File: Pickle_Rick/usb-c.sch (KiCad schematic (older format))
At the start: 3 parts

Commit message: updated optocoupler, usb kinda weird atm ¯\_(ツ)_/¯
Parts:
- removed J?: USB_C_Receptacle_USB2.0, symbol Connector:USB_C_Receptacle_USB2.0
- added R? (x2): 5.1k, symbol Device:R
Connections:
- net labels added: usb_DETONATOR
- net labels removed: usb_ID
- wire segments 24 -> 21
- no-connect marks 4 -> 2
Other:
- note added: "How it was before"
- note added: "Might do a thing..."
- note added: "d+"
- note added: "d-"
- note added: "detonator\n"
- note added: "tought id was for "device identification"?\n"
- note added: "vbus"
- note removed: "One of these is right for sure..."
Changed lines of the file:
@@
 L Connector:USB_B_Micro J?
 U 1 1 6049A0C6
-P 2100 3650
+P 1550 3050
 AR Path="/6049A0C6" Ref="J?"  Part="1"
 AR Path="/602F075A/6049A0C6" Ref="J?"  Part="1"
-F 0 "J?" H 2157 4117 50  0000 C CNN
-F 1 "USB_B_Micro" H 2157 4026 50  0000 C CNN
-F 2 "Connector_USB:USB_Micro-B_Amphenol_10103594-0001LF_Horizontal" H 2250 3600 50  0001 C CNN
-F 3 "~" H 2250 3600 50  0001 C CNN
-	1    2100 3650
+F 0 "J?" H 1607 3517 50  0000 C CNN
+F 1 "USB_B_Micro" H 1607 3426 50  0000 C CNN
+F 2 "Connector_USB:USB_Micro-B_Amphenol_10103594-0001LF_Horizontal" H 1700 3000 50  0001 C CNN
+F 3 "~" H 1700 3000 50  0001 C CNN
+	1    1550 3050
 	1    0    0    -1
 $EndComp
-Connection ~ 2100 4050
+Connection ~ 1550 3450
 $Comp
 L power:GND #PWR?
 U 1 1 6049A0CD
-P 2100 4150
+P 1550 3550
 AR Path="/6049A0CD" Ref="#PWR?"  Part="1"
 AR Path="/602F075A/6049A0CD" Ref="#PWR?"  Part="1"
-F 0 "#PWR?" H 2100 3900 50  0001 C CNN
-F 1 "GND" H 2105 3977 50  0000 C CNN
-F 2 "" H 2100 4150 50  0001 C CNN
-F 3 "" H 2100 4150 50  0001 C CNN
-	1    2100 4150
+F 0 "#PWR?" H 1550 3300 50  0001 C CNN
+F 1 "GND" H 1555 3377 50  0000 C CNN
+F 2 "" H 1550 3550 50  0001 C CNN
+F 3 "" H 1550 3550 50  0001 C CNN
+	1    1550 3550
 	1    0    0    -1
 $EndComp
 Wire Wire Line
-	2100 4150 2100 4050
+	1550 3550 1550 3450
 Wire Wire Line
-	2100 4050 2000 4050
+	1550 3450 1450 3450
 Text HLabel 5400 2700 2    50   Input ~ 0
 usb_VBUS
 Wire Wire Line
-	2400 3650 2900 3650
+	1850 3050 2350 3050
 Wire Wire Line
-	2400 3750 2900 3750
+	1850 3150 2350 3150
 Wire Wire Line
-	2900 3850 2400 3850
+	2350 3250 1850 3250
 Wire Wire Line
-	2400 3450 2900 3450
+	1850 2850 2350 2850
 Wire Wire Line
 	4700 2700 5400 2700
@@
 $EndComp
 Wire Wire Line
+	4100 4350 4100 4200
+NoConn ~ 4700 3800
+NoConn ~ 4700 3900
+Connection ~ 4100 4200
+Connection ~ 4700 3200
+Connection ~ 4700 3500
+Wire Wire Line
 	3800 4200 4100 4200
-Wire Wire Line
-	4100 4350 4100 4200
-Connection ~ 4700 3500
-Connection ~ 4700 3200
-Connection ~ 4100 4200
 $Comp
 L Connector:USB_C_Receptacle_USB2.0 J?
@@
 	1    0    0    -1
 $EndComp
-Text HLabel 5450 2900 2    50   Input ~ 0
-usb_ID
-NoConn ~ 4700 3800
-NoConn ~ 4700 3900
-Wire Wire Line
-	4700 3000 4700 2900
-Wire Wire Line
-	5450 2900 4700 2900
-Connection ~ 4700 2900
-Text HLabel 8400 3500 2    50   Input ~ 0
-usb_D+
-Text HLabel 8400 3200 2    50   Input ~ 0
-usb_D-
-Text HLabel 8350 2700 2    50   Input ~ 0
-usb_VBUS
-Wire Wire Line
-	7650 2700 8350 2700
-Wire Wire Line
-	7650 3200 7650 3300
-Wire Wire Line
-	7650 3200 8400 3200
-Wire Wire Line
-	7650 3400 7650 3500
-Wire Wire Line
-	8400 3500 7650 3500
 $Comp
 L power:GND #PWR?
-U 1 1 60743CCA
-P 7050 4350
-F 0 "#PWR?" H 7050 4100 50  0001 C CNN
-F 1 "GND" H 7055 4177 50  0000 C CNN
-F 2 "" H 7050 4350 50  0001 C CNN
-F 3 "" H 7050 4350 50  0001 C CNN
-	1    7050 4350
-	1    0    0    -1
+U 1 1 6043327D
+P 6400 2850
+F 0 "#PWR?" H 6400 2600 50  0001 C CNN
+F 1 "GND" V 6405 2722 50  0000 R CNN
+F 2 "" H 6400 2850 50  0001 C CNN
+F 3 "" H 6400 2850 50  0001 C CNN
+	1    6400 2850
+	0    -1   -1   0
+$EndComp
+$Comp
+L power:GND #PWR?
+U 1 1 604354EC
+P 6400 3050
+F 0 "#PWR?" H 6400 2800 50  0001 C CNN
+F 1 "GND" V 6405 2922 50  0000 R CNN
+F 2 "" H 6400 3050 50  0001 C CNN
+F 3 "" H 6400 3050 50  0001 C CNN
+	1    6400 3050
+	0    -1   -1   0
+$EndComp
+$Comp
+L Device:R R?
+U 1 1 6043A0B1
+P 6050 2850
+F 0 "R?" V 5843 2850 50  0000 C CNN
+F 1 "5.1k" V 5934 2850 50  0000 C CNN
+F 2 "" V 5980 2850 50  0001 C CNN
+F 3 "~" H 6050 2850 50  0001 C CNN
+	1    6050 2850
+	0    1    1    0
+$EndComp
+$Comp
+L Device:R R?
+U 1 1 6043AE1B
+P 6050 3050
+F 0 "R?" V 6257 3050 50  0000 C CNN
+F 1 "5.1k" V 6166 3050 50  0000 C CNN
+F 2 "" V 5980 3050 50  0001 C CNN
+F 3 "~" H 6050 3050 50  0001 C CNN
+	1    6050 3050
+	0    -1   -1   0
 $EndComp
 Wire Wire Line
-	6750 4200 7050 4200
+	4700 2900 5800 2900
 Wire Wire Line
-	7050 4350 7050 4200
-Text HLabel 8600 3900 2    50   Input ~ 0
-usb_ID
-Connection ~ 7650 3500
-Connection ~ 7650 3200
-Connection ~ 7050 4200
-$Comp
-L Connector:USB_C_Receptacle_USB2.0 J?
-U 1 1 60743CD5
-P 7050 3300
-F 0 "J?" H 7157 4167 50  0000 C CNN
-F 1 "USB_C_Receptacle_USB2.0" H 7157 4076 50  0000 C CNN
-F 2 "" H 7200 3300 50  0001 C CNN
-F 3 "https://www.usb.org/sites/default/files/documents/usb_type-c.zip" H 7200 3300 50  0001 C CNN
-	1    7050 3300
-	1    0    0    -1
-$EndComp
-NoConn ~ 7650 2900
-NoConn ~ 7650 3000
+	5800 2900 5800 2850
 Wire Wire Line
-	7650 3800 7650 3900
+	5800 2850 5900 2850
 Wire Wire Line
-	7650 3900 8600 3900
-Connection ~ 7650 3900
-Text Notes 4900 2300 0    89   ~ 0
-One of these is right for sure...
+	6200 2850 6400 2850
+Wire Wire Line
+	6400 3050 6200 3050
+Wire Wire Line
+	5900 3050 5800 3050
+Wire Wire Line
+	5800 3050 5800 3000
+Wire Wire Line
+	5800 3000 4700 3000
+Text Notes 1300 2500 0    50   ~ 0
+How it was before
+Text Notes 3700 2300 0    50   ~ 0
+Might do a thing...
+Text Notes 2450 2850 0    50   ~ 0
+vbus
+Text Notes 2450 3050 0    50   ~ 0
+d+
+Text Notes 2450 3150 0    50   ~ 0
+d-
+Text Notes 2450 3300 0    50   ~ 0
+detonator\n
+Text HLabel 5500 3700 2    50   Input ~ 0
+usb_DETONATOR
+Text Notes 1600 3500 0    50   ~ 0
+tought id was for "device identification"?\n
 $EndSCHEMATC

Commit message: 50/50 that the usb will work
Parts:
- removed J?: USB_B_Micro, Connector_USB:USB_Micro-B_Amphenol_10103594-0001LF_Horizontal, symbol Connector:USB_B_Micro
- R41, R42: renamed from R?; footprint (none) -> Resistor_SMD:R_0603_1608Metric
- gave numbers to parts that had none: 1
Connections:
- wire segments 21 -> 15
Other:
- note removed: "How it was before"
- note removed: "Might do a thing..."
- note removed: "d+"
- note removed: "d-"
- note removed: "detonator\n"
- note removed: "tought id was for "device identification"?\n"
- note removed: "vbus"
- moved on the sheet: R41, R42
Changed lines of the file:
@@
 Text HLabel 5450 3200 2    50   Input ~ 0
 usb_D-
-$Comp
-L Connector:USB_B_Micro J?
-U 1 1 6049A0C6
-P 1550 3050
-AR Path="/6049A0C6" Ref="J?"  Part="1"
-AR Path="/602F075A/6049A0C6" Ref="J?"  Part="1"
-F 0 "J?" H 1607 3517 50  0000 C CNN
-F 1 "USB_B_Micro" H 1607 3426 50  0000 C CNN
-F 2 "Connector_USB:USB_Micro-B_Amphenol_10103594-0001LF_Horizontal" H 1700 3000 50  0001 C CNN
-F 3 "~" H 1700 3000 50  0001 C CNN
-	1    1550 3050
-	1    0    0    -1
-$EndComp
-Connection ~ 1550 3450
-$Comp
-L power:GND #PWR?
-U 1 1 6049A0CD
-P 1550 3550
-AR Path="/6049A0CD" Ref="#PWR?"  Part="1"
-AR Path="/602F075A/6049A0CD" Ref="#PWR?"  Part="1"
-F 0 "#PWR?" H 1550 3300 50  0001 C CNN
-F 1 "GND" H 1555 3377 50  0000 C CNN
-F 2 "" H 1550 3550 50  0001 C CNN
-F 3 "" H 1550 3550 50  0001 C CNN
-	1    1550 3550
-	1    0    0    -1
-$EndComp
-Wire Wire Line
-	1550 3550 1550 3450
-Wire Wire Line
-	1550 3450 1450 3450
 Text HLabel 5400 2700 2    50   Input ~ 0
 usb_VBUS
-Wire Wire Line
-	1850 3050 2350 3050
-Wire Wire Line
-	1850 3150 2350 3150
-Wire Wire Line
-	2350 3250 1850 3250
-Wire Wire Line
-	1850 2850 2350 2850
-Wire Wire Line
-	4700 2700 5400 2700
 Wire Wire Line
 	4700 3200 4700 3300
@@
 	5450 3500 4700 3500
 $Comp
-L power:GND #PWR?
+L power:GND #PWR0110
 U 1 1 60735E2B
 P 4100 4350
-F 0 "#PWR?" H 4100 4100 50  0001 C CNN
+F 0 "#PWR0110" H 4100 4100 50  0001 C CNN
 F 1 "GND" H 4105 4177 50  0000 C CNN
 F 2 "" H 4100 4350 50  0001 C CNN
@@
 	3800 4200 4100 4200
 $Comp
-L Connector:USB_C_Receptacle_USB2.0 J?
+L Connector:USB_C_Receptacle_USB2.0 J1
 U 1 1 607282EC
 P 4100 3300
-F 0 "J?" H 4207 4167 50  0000 C CNN
+F 0 "J1" H 4207 4167 50  0000 C CNN
 F 1 "USB_C_Receptacle_USB2.0" H 4207 4076 50  0000 C CNN
 F 2 "" H 4250 3300 50  0001 C CNN
@@
 $EndComp
 $Comp
-L power:GND #PWR?
-U 1 1 6043327D
-P 6400 2850
-F 0 "#PWR?" H 6400 2600 50  0001 C CNN
-F 1 "GND" V 6405 2722 50  0000 R CNN
-F 2 "" H 6400 2850 50  0001 C CNN
-F 3 "" H 6400 2850 50  0001 C CNN
-	1    6400 2850
-	0    -1   -1   0
-$EndComp
-$Comp
-L power:GND #PWR?
-U 1 1 604354EC
-P 6400 3050
-F 0 "#PWR?" H 6400 2800 50  0001 C CNN
-F 1 "GND" V 6405 2922 50  0000 R CNN
-F 2 "" H 6400 3050 50  0001 C CNN
-F 3 "" H 6400 3050 50  0001 C CNN
-	1    6400 3050
-	0    -1   -1   0
-$EndComp
-$Comp
-L Device:R R?
+L Device:R R42
 U 1 1 6043A0B1
-P 6050 2850
-F 0 "R?" V 5843 2850 50  0000 C CNN
-F 1 "5.1k" V 5934 2850 50  0000 C CNN
-F 2 "" V 5980 2850 50  0001 C CNN
-F 3 "~" H 6050 2850 50  0001 C CNN
-	1    6050 2850
-	0    1    1    0
-$EndComp
-$Comp
-L Device:R R?
-U 1 1 6043AE1B
-P 6050 3050
-F 0 "R?" V 6257 3050 50  0000 C CNN
-F 1 "5.1k" V 6166 3050 50  0000 C CNN
-F 2 "" V 5980 3050 50  0001 C CNN
-F 3 "~" H 6050 3050 50  0001 C CNN
-	1    6050 3050
-	0    -1   -1   0
+P 7100 3150
+F 0 "R42" V 6893 3150 50  0000 C CNN
+F 1 "5.1k" V 6984 3150 50  0000 C CNN
+F 2 "Resistor_SMD:R_0603_1608Metric" V 7030 3150 50  0001 C CNN
+F 3 "~" H 7100 3150 50  0001 C CNN
+	1    7100 3150
+	-1   0    0    1
 $EndComp
 Wire Wire Line
-	4700 2900 5800 2900
+	6600 3500 6600 3300
+Text HLabel 6850 3900 2    50   Input ~ 0
+usb_DETONATOR
 Wire Wire Line
-	5800 2900 5800 2850
+	7100 2900 7100 3000
 Wire Wire Line
-	5800 2850 5900 2850
+	4700 2700 5400 2700
+$Comp
+L Device:R R41
+U 1 1 6043AE1B
+P 6600 3150
+F 0 "R41" V 6807 3150 50  0000 C CNN
+F 1 "5.1k" V 6716 3150 50  0000 C CNN
+F 2 "Resistor_SMD:R_0603_1608Metric" V 6530 3150 50  0001 C CNN
+F 3 "~" H 6600 3150 50  0001 C CNN
+	1    6600 3150
+	1    0    0    -1
+$EndComp
 Wire Wire Line
-	6200 2850 6400 2850
+	4700 2900 7100 2900
 Wire Wire Line
-	6400 3050 6200 3050
+	4700 3000 6600 3000
 Wire Wire Line
-	5900 3050 5800 3050
+	6600 3500 6850 3500
 Wire Wire Line
-	5800 3050 5800 3000
+	7100 3300 7100 3500
 Wire Wire Line
-	5800 3000 4700 3000
-Text Notes 1300 2500 0    50   ~ 0
-How it was before
-Text Notes 3700 2300 0    50   ~ 0
-Might do a thing...
-Text Notes 2450 2850 0    50   ~ 0
-vbus
-Text Notes 2450 3050 0    50   ~ 0
-d+
-Text Notes 2450 3150 0    50   ~ 0
-d-
-Text Notes 2450 3300 0    50   ~ 0
-detonator\n
-Text HLabel 5500 3700 2    50   Input ~ 0
-usb_DETONATOR
-Text Notes 1600 3500 0    50   ~ 0
-tought id was for "device identification"?\n
+	6850 3500 6850 3900
+Connection ~ 6850 3500
+Wire Wire Line
+	6850 3500 7100 3500
 $EndSCHEMATC

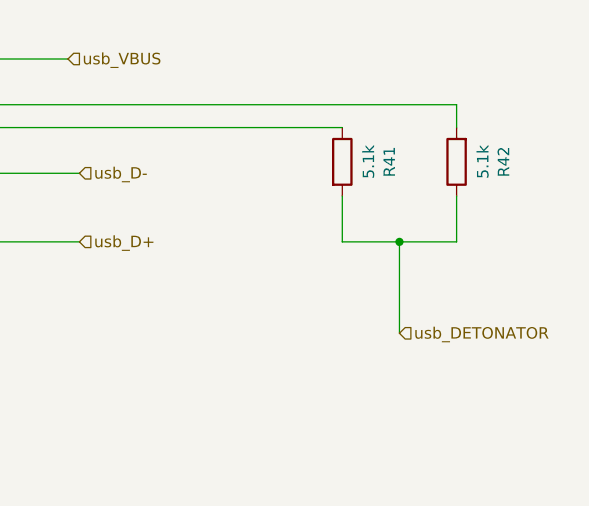
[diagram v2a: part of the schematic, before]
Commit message: fixed led circuit/made sure cc pins are independent
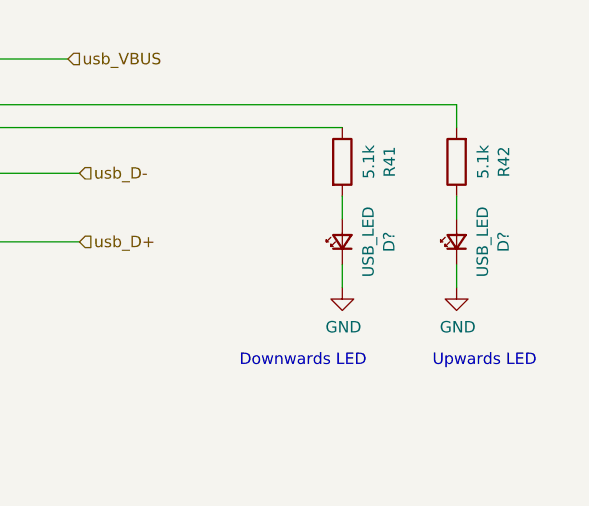
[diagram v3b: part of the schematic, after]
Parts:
- added D? (x2): USB_LED, LED_SMD:LED_0603_1608Metric_Castellated, symbol Device:LED_Small
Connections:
- net GND: now also D?.1 (K), D?.1 (K)
- net usb_DETONATOR: no longer names the net of R42.1
- net usb_DETONATOR: now also D?.2 (A); no longer R41.2
- new net: D?.2 (A), R41.2
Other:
- note added: "Downwards LED"
- note added: "Upwards LED"
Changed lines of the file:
@@
 $EndComp
-Wire Wire Line
-	6600 3500 6600 3300
-Text HLabel 6850 3900 2    50   Input ~ 0
-usb_DETONATOR
 Wire Wire Line
 	7100 2900 7100 3000
@@
 Wire Wire Line
 	4700 3000 6600 3000
+$Comp
+L power:GND #PWR?
+U 1 1 60488D63
+P 6600 3700
+F 0 "#PWR?" H 6600 3450 50  0001 C CNN
+F 1 "GND" H 6605 3527 50  0000 C CNN
+F 2 "" H 6600 3700 50  0001 C CNN
+F 3 "" H 6600 3700 50  0001 C CNN
+	1    6600 3700
+	1    0    0    -1
+$EndComp
+$Comp
+L power:GND #PWR?
+U 1 1 60489008
+P 7100 3700
+F 0 "#PWR?" H 7100 3450 50  0001 C CNN
+F 1 "GND" H 7105 3527 50  0000 C CNN
+F 2 "" H 7100 3700 50  0001 C CNN
+F 3 "" H 7100 3700 50  0001 C CNN
+	1    7100 3700
+	1    0    0    -1
+$EndComp
+$Comp
+L Device:LED_Small D?
+U 1 1 6053D295
+P 6600 3500
+AR Path="/6053D295" Ref="D?"  Part="1"
+AR Path="/602F075A/6053D295" Ref="D?"  Part="1"
+F 0 "D?" H 6600 3295 50  0000 C CNN
+F 1 "USB_LED" H 6600 3386 50  0000 C CNN
+F 2 "LED_SMD:LED_0603_1608Metric_Castellated" V 6600 3500 50  0001 C CNN
+F 3 "~" V 6600 3500 50  0001 C CNN
+	1    6600 3500
+	0    -1   -1   0
+$EndComp
 Wire Wire Line
-	6600 3500 6850 3500
+	6600 3300 6600 3400
 Wire Wire Line
-	7100 3300 7100 3500
+	6600 3600 6600 3700
 Wire Wire Line
-	6850 3500 6850 3900
-Connection ~ 6850 3500
+	7100 3700 7100 3600
+$Comp
+L Device:LED_Small D?
+U 1 1 604A9E91
+P 7100 3500
+AR Path="/604A9E91" Ref="D?"  Part="1"
+AR Path="/602F075A/604A9E91" Ref="D?"  Part="1"
+F 0 "D?" H 7100 3295 50  0000 C CNN
+F 1 "USB_LED" H 7100 3386 50  0000 C CNN
+F 2 "LED_SMD:LED_0603_1608Metric_Castellated" V 7100 3500 50  0001 C CNN
+F 3 "~" V 7100 3500 50  0001 C CNN
+	1    7100 3500
+	0    -1   -1   0
+$EndComp
 Wire Wire Line
-	6850 3500 7100 3500
+	7100 3400 7100 3300
+Text Notes 7450 4050 2    50   ~ 0
+Upwards LED
+Text Notes 6150 4050 0    50   ~ 0
+Downwards LED
 $EndSCHEMATC

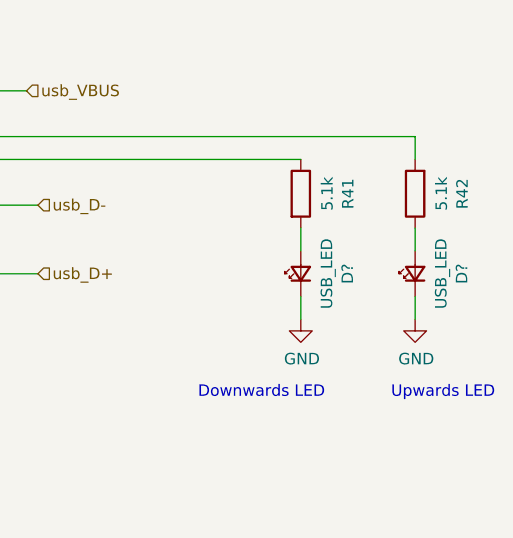
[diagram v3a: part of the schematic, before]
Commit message: changed to single 2 channel optocoupler
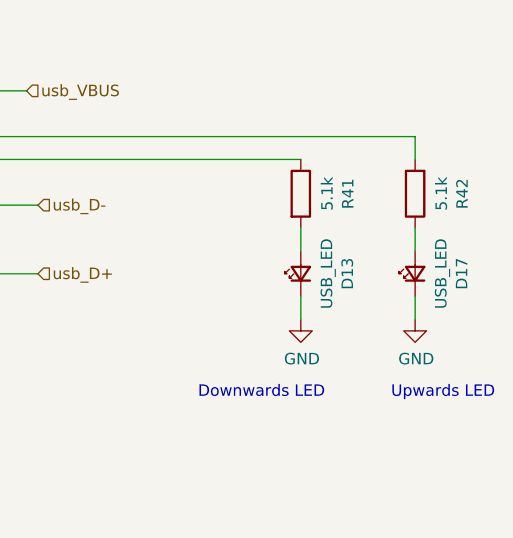
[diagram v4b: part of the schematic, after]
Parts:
- gave numbers to parts that had none: 2
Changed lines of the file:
@@
 	4700 3000 6600 3000
 $Comp
-L power:GND #PWR?
+L power:GND #PWR01
 U 1 1 60488D63
 P 6600 3700
-F 0 "#PWR?" H 6600 3450 50  0001 C CNN
+F 0 "#PWR01" H 6600 3450 50  0001 C CNN
 F 1 "GND" H 6605 3527 50  0000 C CNN
 F 2 "" H 6600 3700 50  0001 C CNN
@@
 $EndComp
 $Comp
-L power:GND #PWR?
+L power:GND #PWR055
 U 1 1 60489008
 P 7100 3700
-F 0 "#PWR?" H 7100 3450 50  0001 C CNN
+F 0 "#PWR055" H 7100 3450 50  0001 C CNN
 F 1 "GND" H 7105 3527 50  0000 C CNN
 F 2 "" H 7100 3700 50  0001 C CNN
@@
 P 6600 3500
 AR Path="/6053D295" Ref="D?"  Part="1"
-AR Path="/602F075A/6053D295" Ref="D?"  Part="1"
-F 0 "D?" H 6600 3295 50  0000 C CNN
+AR Path="/602F075A/6053D295" Ref="D13"  Part="1"
+F 0 "D13" H 6600 3295 50  0000 C CNN
 F 1 "USB_LED" H 6600 3386 50  0000 C CNN
 F 2 "LED_SMD:LED_0603_1608Metric_Castellated" V 6600 3500 50  0001 C CNN
@@
 P 7100 3500
 AR Path="/604A9E91" Ref="D?"  Part="1"
-AR Path="/602F075A/604A9E91" Ref="D?"  Part="1"
-F 0 "D?" H 7100 3295 50  0000 C CNN
+AR Path="/602F075A/604A9E91" Ref="D17"  Part="1"
+F 0 "D17" H 7100 3295 50  0000 C CNN
 F 1 "USB_LED" H 7100 3386 50  0000 C CNN
 F 2 "LED_SMD:LED_0603_1608Metric_Castellated" V 7100 3500 50  0001 C CNN
